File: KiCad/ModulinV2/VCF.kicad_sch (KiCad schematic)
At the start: 74 parts, among them IC54 AS3320D, IC55 TL072HIDR, IC56 AS3320D

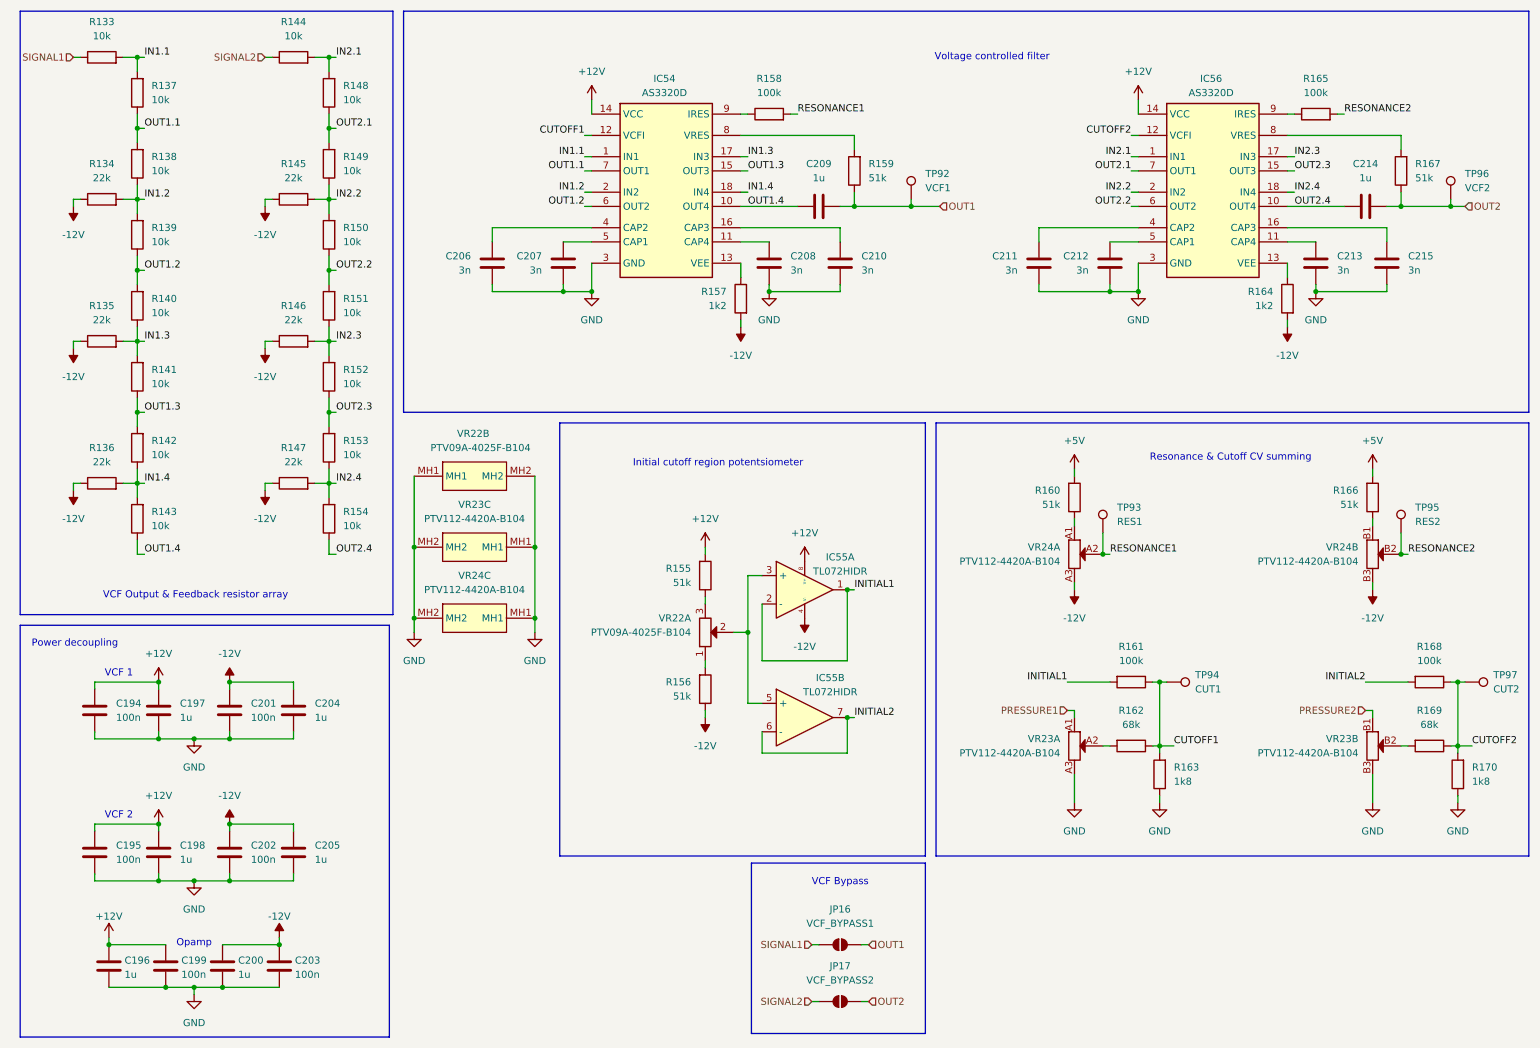
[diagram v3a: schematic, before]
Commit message: Completed tuning & mod wheel layouts
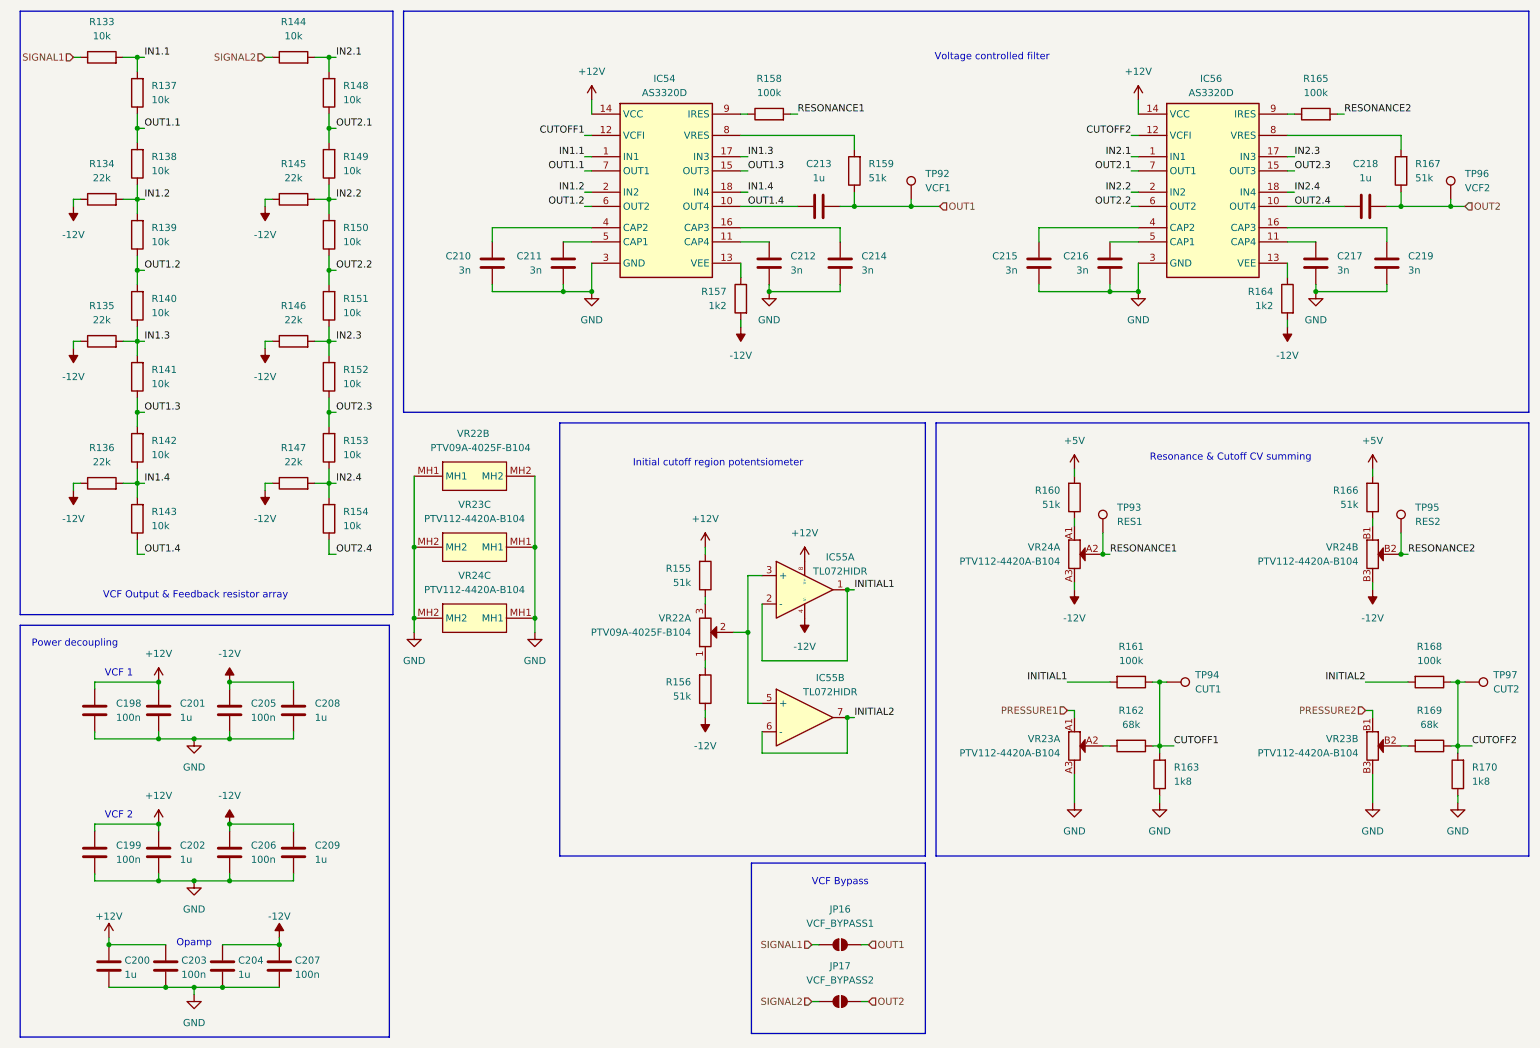
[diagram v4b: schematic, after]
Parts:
- renumbered C194 to C198, C195 to C199, C196 to C200, C197 to C201, C198 to C202, C199 to C203, C200 to C204, C201 to C205, C202 to C206, C203 to C207, C204 to C208, C205 to C209, C206 to C210, C207 to C211, C208 to C212, C209 to C213, C210 to C214, C211 to C215, C212 to C216, C213 to C217, C214 to C218, C215 to C219

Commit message: Fixed schematic connections
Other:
- company: (none) -> TalTech
- title: (none) -> Voltage Controlled Filter
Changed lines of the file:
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@@
 	(paper "A4")
 	(title_block
+		(title "Voltage Controlled Filter")
+		(date "2026-04-29")
+		(rev "1.4")
+		(company "TalTech")
 		(comment 1 "Instructor: Kaiser Pärnamets")
-		(comment 2 "By: Rasmus Palk")
+		(comment 2 "Author: Rasmus Palk")
 	)
 	(rectangle
